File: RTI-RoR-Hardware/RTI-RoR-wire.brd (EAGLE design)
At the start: 80 x 71.1 mm, 32 parts, among them IC2 74LVC244

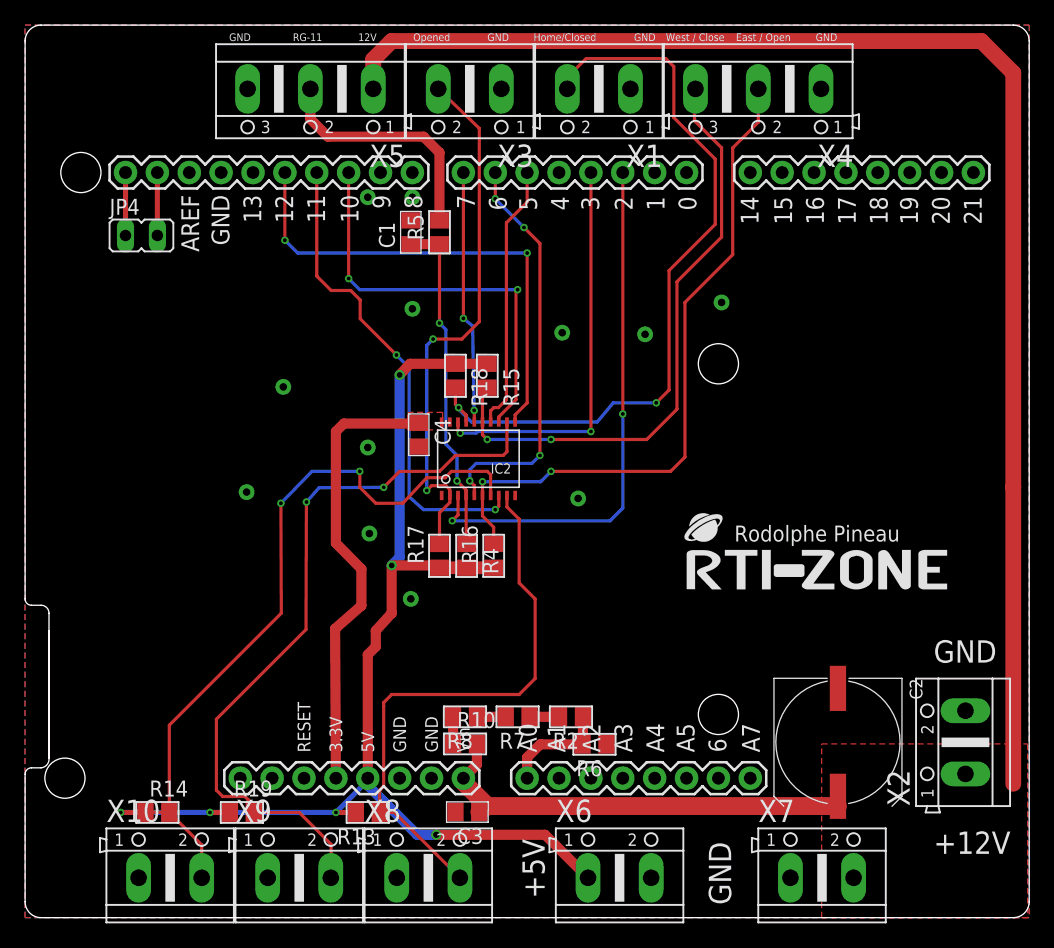
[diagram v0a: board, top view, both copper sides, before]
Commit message: Adding the at park pins to both PCB for the Arduino DUE.
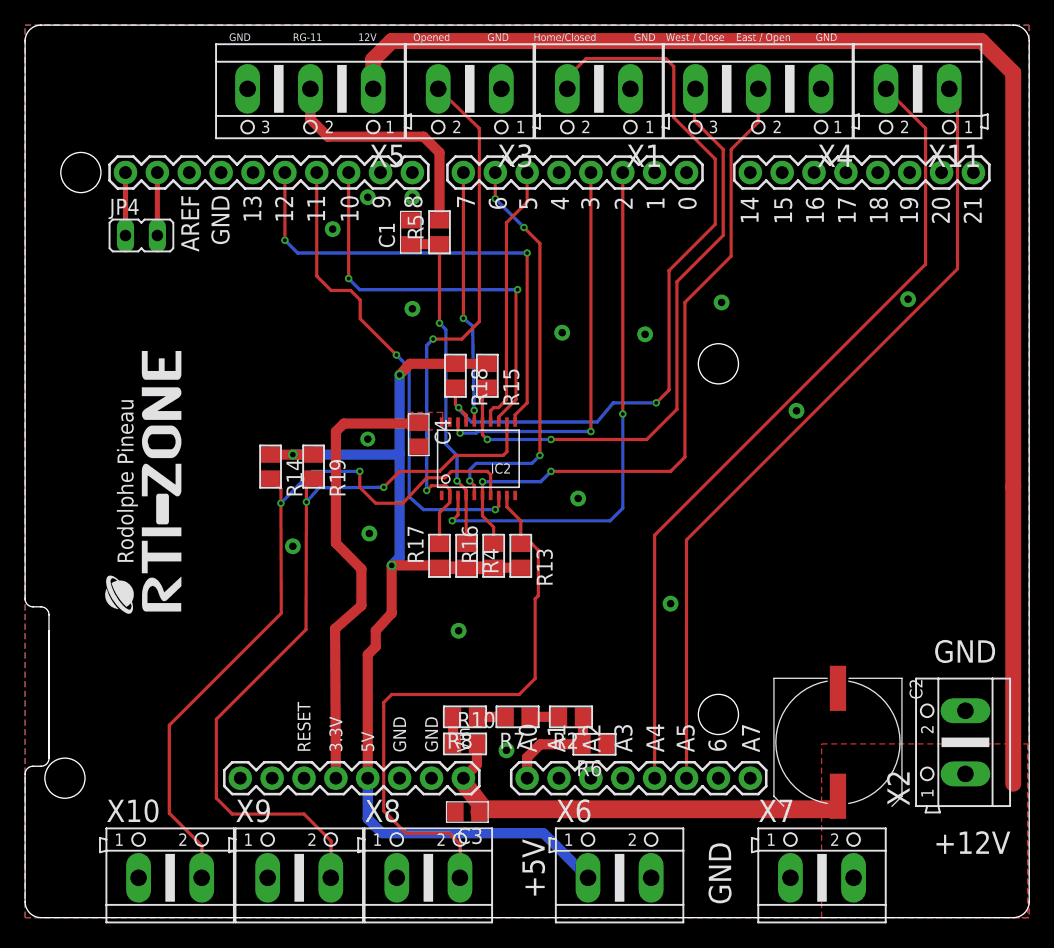
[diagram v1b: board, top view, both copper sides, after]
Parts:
- added X11: (no value), con-ptr500:AK500/2
- moved U$4 40.3 mm to (12.4, 24.4), turned to 90 degrees
- moved R14 29.0 mm to (19.6, 35.9), turned to 270 degrees
- moved R19 28.1 mm to (23.0, 35.9), turned to 270 degrees
- moved R13 23.8 mm to (39.5, 28.8), turned to 270 degrees
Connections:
- removed net XBEE_DOUT: PCB1.19
- new net AT_PARK_PIN: PCB1.A5, X11.1
- new net AT_PARK_PIN_LOOP: PCB1.A4, X11.2
- new net XBEE_RESET: PCB1.8
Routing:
- net AT_PARK_PIN_LOOP: track 0.00 -> 65.2 mm
- net AT_PARK_PIN: track 0.00 -> 64.1 mm
- net VCC: track 95.8 -> 85.6 mm, vias 6 -> 3
- net M_DIR_5V: track 59.9 -> 62.2 mm
- net M_STEP_5V: track 45.8 -> 47.6 mm
- net M_EN_5V: track 60.3 -> 59.4 mm
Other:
- outline, holes or cut-outs redrawn
